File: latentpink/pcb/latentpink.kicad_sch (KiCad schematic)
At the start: 14 parts, among them M3 SCREWHOLE, M4 SCREWHOLE, M5 SCREWHOLE, M6 SCREWHOLE

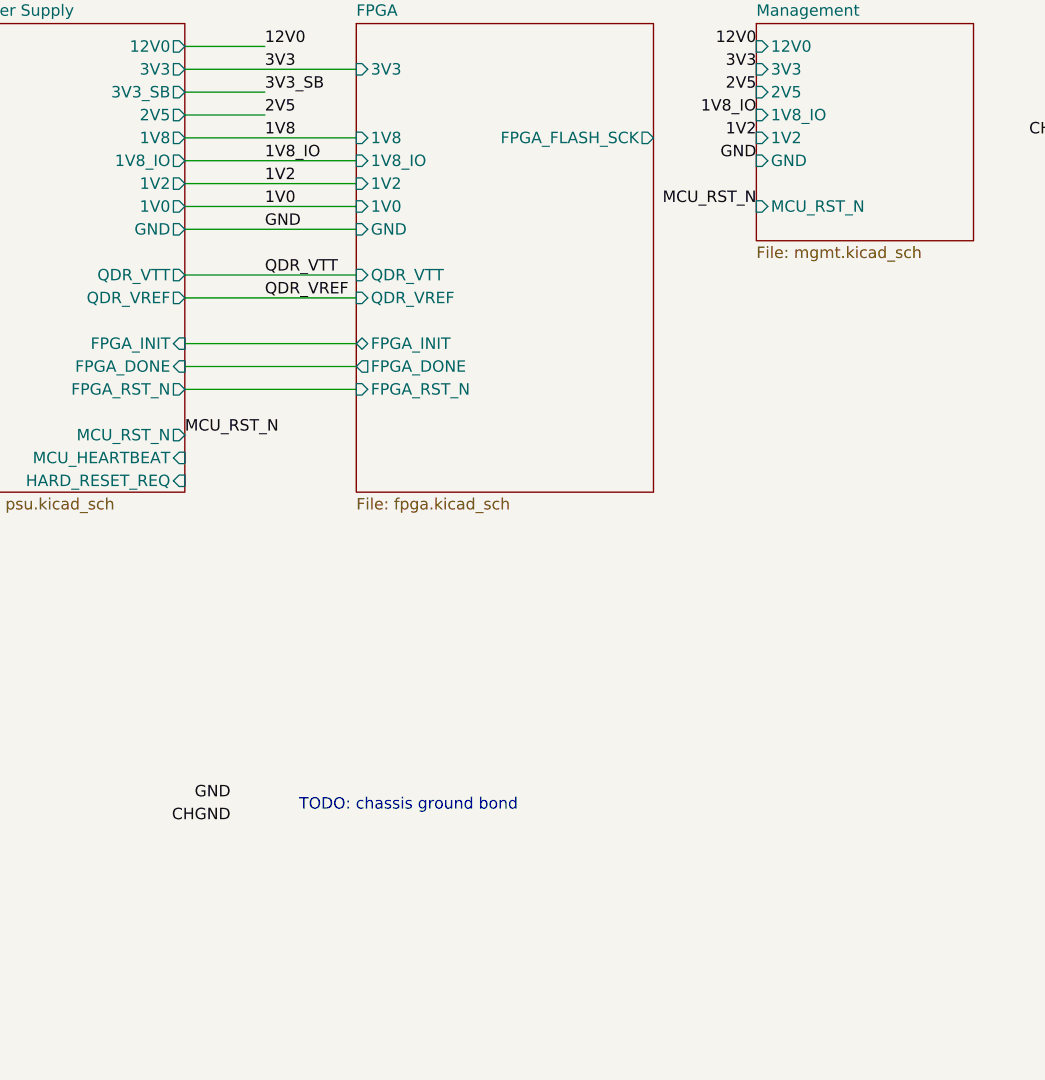
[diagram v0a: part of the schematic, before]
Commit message: Continued initial component placement
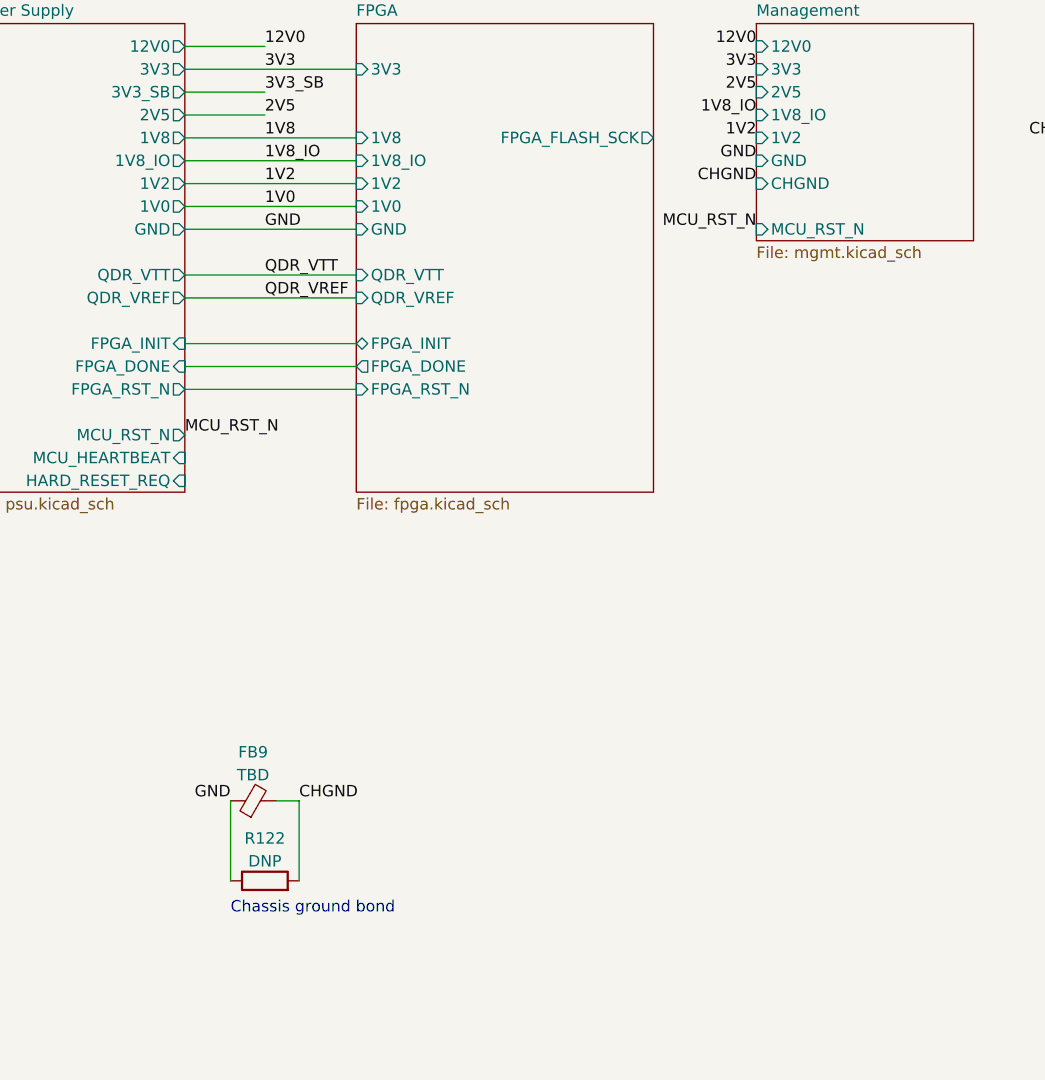
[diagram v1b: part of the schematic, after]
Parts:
- added FB9: TBD, symbol device:Ferrite_Bead_Small
- added R122: DNP, symbol device:R
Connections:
- net CHGND: now also FB9.2, R122.2
- net GND: now also FB9.1, R122.1
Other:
- sheet Management ports: added CHGND; removed none
- note added: "Chassis ground bond"
- note removed: "TODO: chassis ground bond"
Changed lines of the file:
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@@
+    (stroke (width 0) (type default) (color 0 0 0 0))
+  )
+  (wire (pts (xy 74.93 109.22) (xy 77.47 109.22))
     (stroke (width 0) (type default) (color 0 0 0 0))
   )
@@
     (stroke (width 0) (type default) (color 0 0 0 0))
   )
+  (wire (pts (xy 77.47 109.22) (xy 77.47 118.11))
+    (stroke (width 0) (type default) (color 0 0 0 0))
+  )
   (wire (pts (xy 30.48 171.45) (xy 34.29 171.45))
     (stroke (width 0) (type default) (color 0 0 0 0))
@@
     (stroke (width 0) (type default) (color 0 0 0 0))
   )
+  (wire (pts (xy 69.85 109.22) (xy 69.85 118.11))
+    (stroke (width 0) (type default) (color 0 0 0 0))
+  )
   (wire (pts (xy 30.48 190.5) (xy 34.29 190.5))
     (stroke (width 0) (type default) (color 0 0 0 0))
@@
     (stroke (width 0) (type default) (color 0 0 0 0))
   )
-  (text "TODO: chassis ground bond" (at 77.47 110.49 0)
+  (text "Chassis ground bond" (at 69.85 121.92 0)
     (effects (font (size 1.27 1.27)) (justify left bottom))
   )
@@
     (effects (font (size 1.27 1.27)) (justify right bottom))
   )
+  (label "CHGND" (at 128.27 40.64 180)
+    (effects (font (size 1.27 1.27)) (justify right bottom))
+  )
   (label "GND" (at 30.48 200.66 180)
     (effects (font (size 1.27 1.27)) (justify right bottom))
@@
     (effects (font (size 1.27 1.27)) (justify right bottom))
   )
-  (label "MCU_RST_N" (at 128.27 43.18 180)
+  (label "MCU_RST_N" (at 128.27 45.72 180)
     (effects (font (size 1.27 1.27)) (justify right bottom))
   )
@@
     (effects (font (size 1.27 1.27)) (justify left bottom))
   )
-  (label "CHGND" (at 69.85 111.76 180)
-    (effects (font (size 1.27 1.27)) (justify right bottom))
+  (label "CHGND" (at 77.47 109.22 0)
+    (effects (font (size 1.27 1.27)) (justify left bottom))
   )
   (label "QDR_VTT" (at 73.66 50.8 0)
@@
     (pin "2")
   )
+  (symbol (lib_id "device:Ferrite_Bead_Small") (at 72.39 109.22 90) (unit 1)
+    (in_bom yes) (on_board yes) (fields_autoplaced)
+    (property "Reference" "FB9" (id 0) (at 72.3519 103.8184 90))
+    (property "Value" "TBD" (id 1) (at 72.3519 106.3553 90))
+    (property "Footprint" "" (id 2) (at 72.39 110.998 90)
+      (effects (font (size 1.27 1.27)) hide)
+    )
+    (property "Datasheet" "" (id 3) (at 72.39 109.22 0)
+      (effects (font (size 1.27 1.27)) hide)
+    )
+    (pin "1")
+    (pin "2")
+  )
   (symbol (lib_id "conn:CONN_COAXIAL") (at 34.29 135.89 0) (unit 1)
     (in_bom yes) (on_board yes) (fields_autoplaced)
@@
     )
     (property "Datasheet" "" (id 3) (at 34.29 135.89 0)
+      (effects (font (size 1.27 1.27)) hide)
+    )
+    (pin "1")
+    (pin "2")
+  )
+  (symbol (lib_id "device:R") (at 73.66 118.11 90) (unit 1)
+    (in_bom yes) (on_board yes) (fields_autoplaced)
+    (property "Reference" "R122" (id 0) (at 73.66 113.3942 90))
+    (property "Value" "DNP" (id 1) (at 73.66 115.9311 90))
+    (property "Footprint" "" (id 2) (at 73.66 119.888 90)
+      (effects (font (size 1.27 1.27)) hide)
+    )
+    (property "Datasheet" "" (id 3) (at 73.66 118.11 0)
       (effects (font (size 1.27 1.27)) hide)
     )
@@
       (effects (font (size 1.27 1.27)) (justify left))
     )
-    (pin "MCU_RST_N" input (at 128.27 43.18 180)
+    (pin "MCU_RST_N" input (at 128.27 45.72 180)
       (effects (font (size 1.27 1.27)) (justify left))
     )
     (pin "1V8_IO" input (at 128.27 33.02 180)
+      (effects (font (size 1.27 1.27)) (justify left))
+    )
+    (pin "CHGND" input (at 128.27 40.64 180)
       (effects (font (size 1.27 1.27)) (justify left))
     )
@@
       (reference "C228") (unit 1) (value "~") (footprint "")
     )
-    (path "/035a8a96-1dae-486c-a84e-a11c0c87b4ac/626b4a48-b66a-4c2b-9c82-5662baf5dfe0/071574bf-d11a-4118-837c-fb8d1907eb25"
-      (reference "C229") (unit 1) (value "0.1 uF") (footprint "azonenberg_pcb:EIA_0402_CAP_NOSILK")
-    )
     (path "/035a8a96-1dae-486c-a84e-a11c0c87b4ac/626b4a48-b66a-4c2b-9c82-5662baf5dfe0/0b976591-9a80-407c-9a49-3c3e8a86cfe3"
       (reference "C230") (unit 1) (value "4.7 uF") (footprint "azonenberg_pcb:EIA_0603_CAP_NOSILK")
@@
       (reference "C440") (unit 1) (value "0.1 uF") (footprint "azonenberg_pcb:EIA_0402_CAP_NOSILK")
     )
+    (path "/22109ef7-0bd2-46c3-8dd9-ecb52bedcbfa/4965ad48-bbe3-4233-a56b-d6f7409a198c"
+      (reference "C441") (unit 1) (value "0.1 uF") (footprint "azonenberg_pcb:EIA_0402_CAP_NOSILK")
+    )
+    (path "/22109ef7-0bd2-46c3-8dd9-ecb52bedcbfa/d1137d44-c0dc-4bb8-b454-601271c24df3"
+      (reference "C442") (unit 1) (value "0.1 uF") (footprint "azonenberg_pcb:EIA_0402_CAP_NOSILK")
+    )
+    (path "/22109ef7-0bd2-46c3-8dd9-ecb52bedcbfa/f09214cd-357a-4c36-a136-0c1a82a02d59"
+      (reference "C443") (unit 1) (value "0.1 uF") (footprint "azonenberg_pcb:EIA_0402_CAP_NOSILK")
+    )
+    (path "/22109ef7-0bd2-46c3-8dd9-ecb52bedcbfa/7eec881a-45ec-44a4-bb68-c4eb0ac641ac"
+      (reference "C444") (unit 1) (value "0.1 uF") (footprint "azonenberg_pcb:EIA_0402_CAP_NOSILK")
+    )
+    (path "/22109ef7-0bd2-46c3-8dd9-ecb52bedcbfa/312af2e8-35e7-4c46-b3ea-9347fc2a59c6"
+      (reference "C445") (unit 1) (value "0.1 uF") (footprint "azonenberg_pcb:EIA_0402_CAP_NOSILK")
+    )
+    (path "/22109ef7-0bd2-46c3-8dd9-ecb52bedcbfa/737be4d2-c736-4be8-b5bd-29cfc3cd9dfa"
+      (reference "C446") (unit 1) (value "0.1 uF") (footprint "azonenberg_pcb:EIA_0402_CAP_NOSILK")
+    )
     (path "/70fb61fd-2f76-4850-9d6b-7e1d9a86570a/dacf15d0-cabc-4cac-8b1d-8797d78eacd5"
       (reference "D1") (unit 1) (value "GREEN") (footprint "azonenberg_pcb:EIA_0603_LED")
@@
       (reference "FB8") (unit 1) (value "MI0603J601R-10") (footprint "azonenberg_pcb:EIA_0603_INDUCTOR_NOSILK")
     )
+    (path "/86504f66-b90f-45e7-842c-dd5449b4f055"
+      (reference "FB9") (unit 1) (value "TBD") (footprint "")
+    )
     (path "/d0e7363b-23d9-4272-a4d1-0db2834b87f3/4b168103-bbc3-44f6-be18-51ccfcb18e25"
       (reference "J1") (unit 1) (value "CONN_SFP_HOST") (footprint "azonenberg_pcb:CONN_SFP+_AMPHENOL_UE76_A10_2000T")
@@
       (reference "R52") (unit 1) (value "4.7K") (footprint "azonenberg_pcb:EIA_0402_RES_NOSILK")
     )
-    (path "/035a8a96-1dae-486c-a84e-a11c0c87b4ac/626b4a48-b66a-4c2b-9c82-5662baf5dfe0/72c05bf9-0ffe-460b-bbdc-8603a2c29498"
-      (reference "R53") (unit 1) (value "1M") (footprint "azonenberg_pcb:EIA_0402_RES_NOSILK")
-    )
     (path "/035a8a96-1dae-486c-a84e-a11c0c87b4ac/626b4a48-b66a-4c2b-9c82-5662baf5dfe0/a90906dc-fbc9-4585-baaa-c07be24eb1f3"
       (reference "R54") (unit 1) (value "470") (footprint "azonenberg_pcb:EIA_0402_RES_NOSILK")
@@
       (reference "R121") (unit 1) (value "11K 1%") (footprint "")
     )
+    (path "/a53e7caf-d1bd-41a0-9413-bbfa4452a48f"
+      (reference "R122") (unit 1) (value "DNP") (footprint "")
+    )
     (path "/6c4b0638-d970-4292-bc58-db2e1b793524/d5990d76-6ad3-4bfd-a9be-5da547fd1224/4d701df3-1531-4e26-be52-80b3fa172f57"

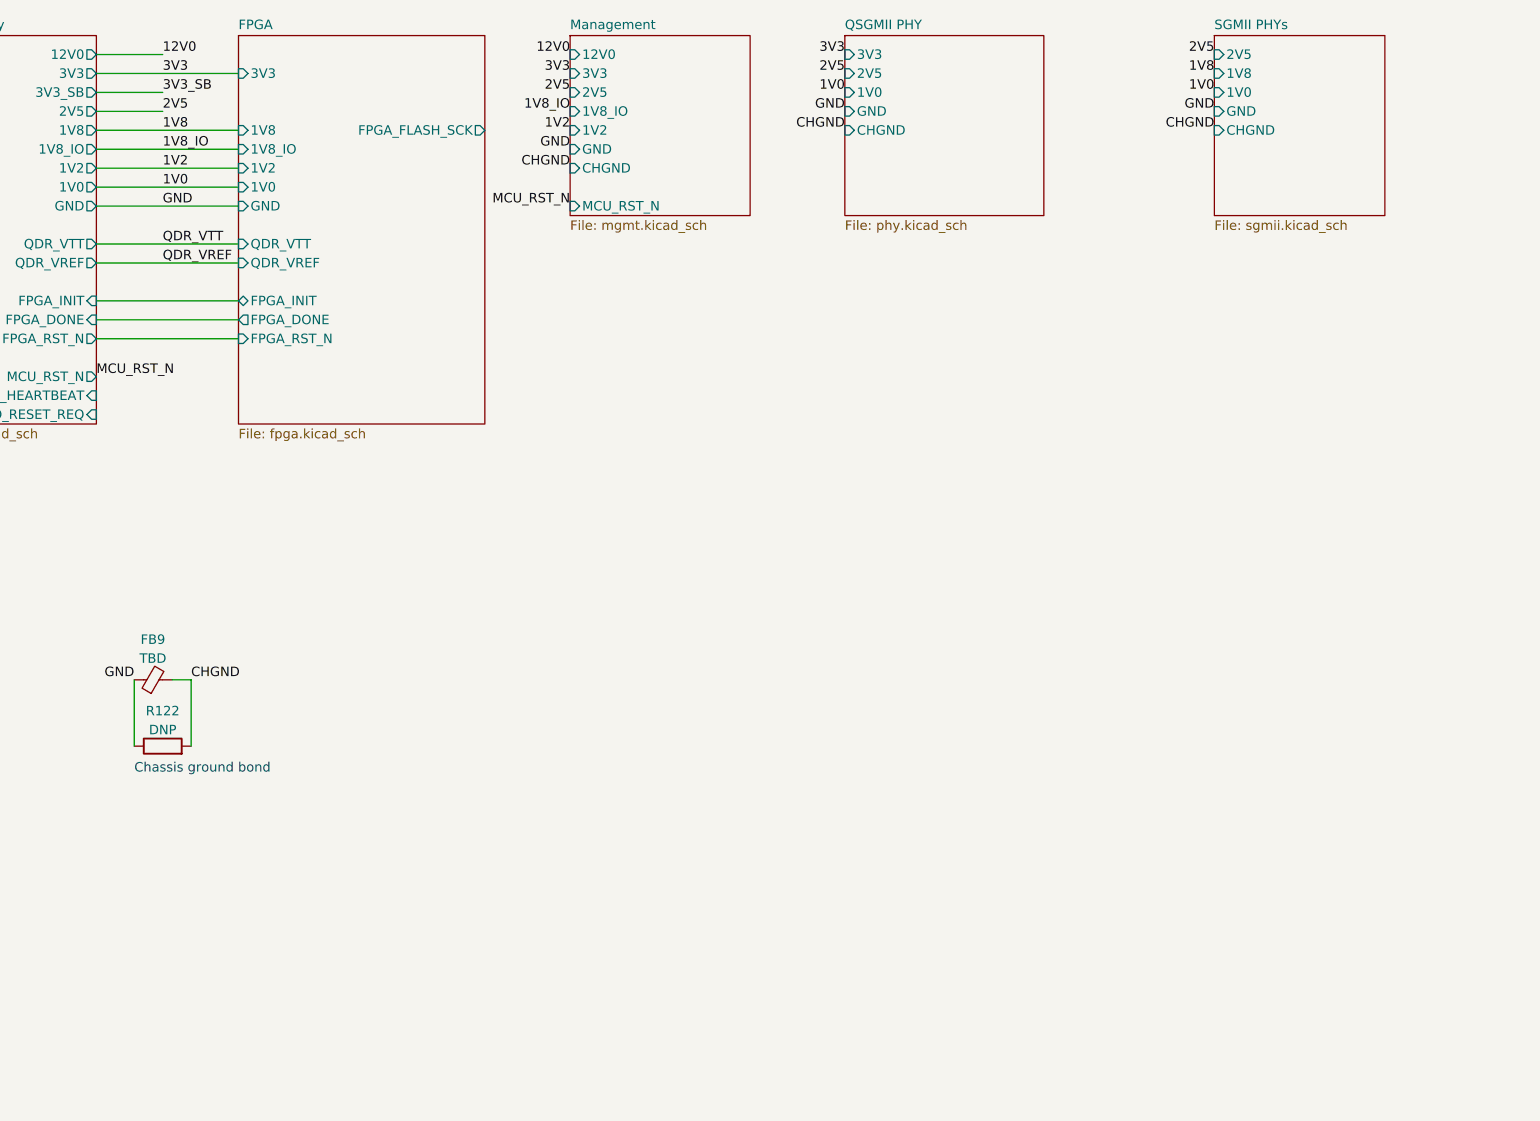
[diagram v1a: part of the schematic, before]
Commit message: Continued footprint assignment and miscellaneous missing tidbits of schematic
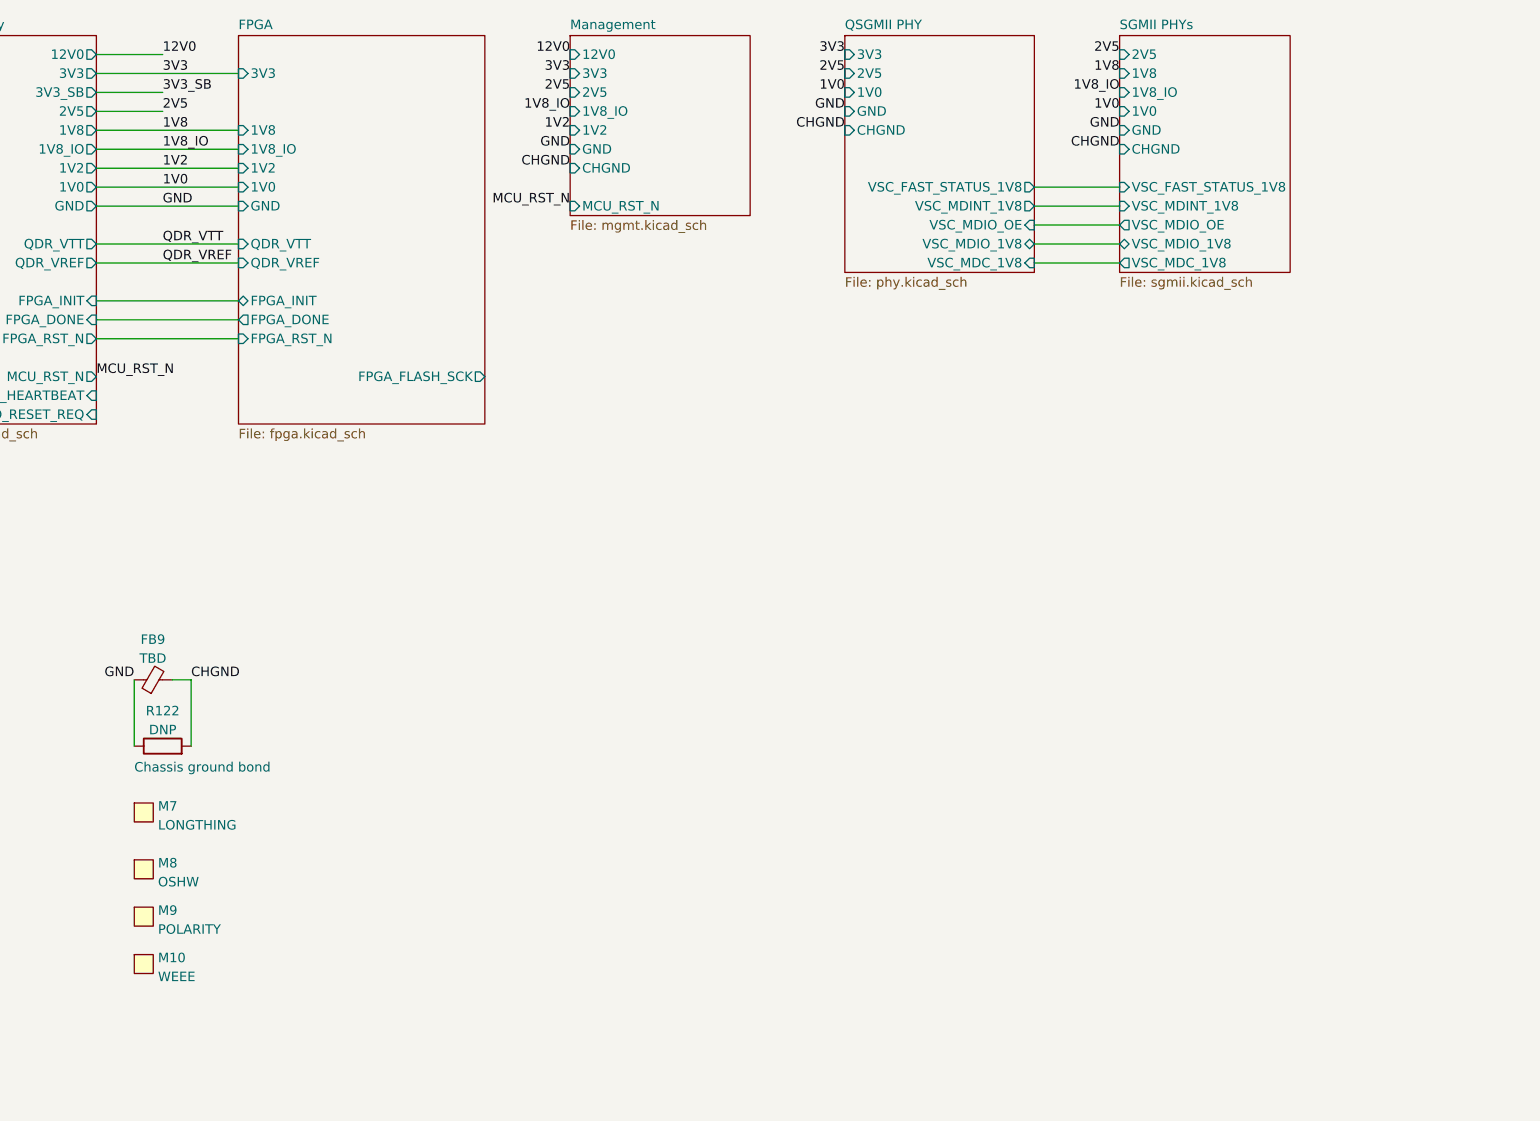
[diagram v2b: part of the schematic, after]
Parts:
- added M10: WEEE, w_logo:Logo_silk_WEEE_3.4x5mm, symbol special-azonenberg:MECHANICAL
- added M7: LONGTHING, azonenberg_pcb:LONGTHING-1200DPI, symbol special-azonenberg:MECHANICAL
- added M8: OSHW, w_logo:Logo_silk_OSHW_6x6mm, symbol special-azonenberg:MECHANICAL
- added M9: POLARITY, w_logo:Logo_silk_polarity_center_5x1.4mm, symbol special-azonenberg:MECHANICAL
- R122: footprint (none) -> azonenberg_pcb:EIA_1206_CAP_NOSILK
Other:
- sheet QSGMII PHY ports: added VSC_FAST_STATUS_1V8, VSC_MDC_1V8, VSC_MDINT_1V8, VSC_MDIO_1V8, VSC_MDIO_OE; removed none
- sheet SGMII PHYs ports: added 1V8_IO, VSC_FAST_STATUS_1V8, VSC_MDC_1V8, VSC_MDINT_1V8, VSC_MDIO_1V8, VSC_MDIO_OE; removed none
